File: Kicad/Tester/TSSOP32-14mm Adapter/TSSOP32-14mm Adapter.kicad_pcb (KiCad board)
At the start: 2 copper layers, 18.3 x 41.4 mm, 4 parts, among them IC1 SST39VF010-70-4I-WHE, J1 Conn_02x16_Counter_Clockwise, J4 Pin_Header_01x16, J5 Pin_Header_01x16

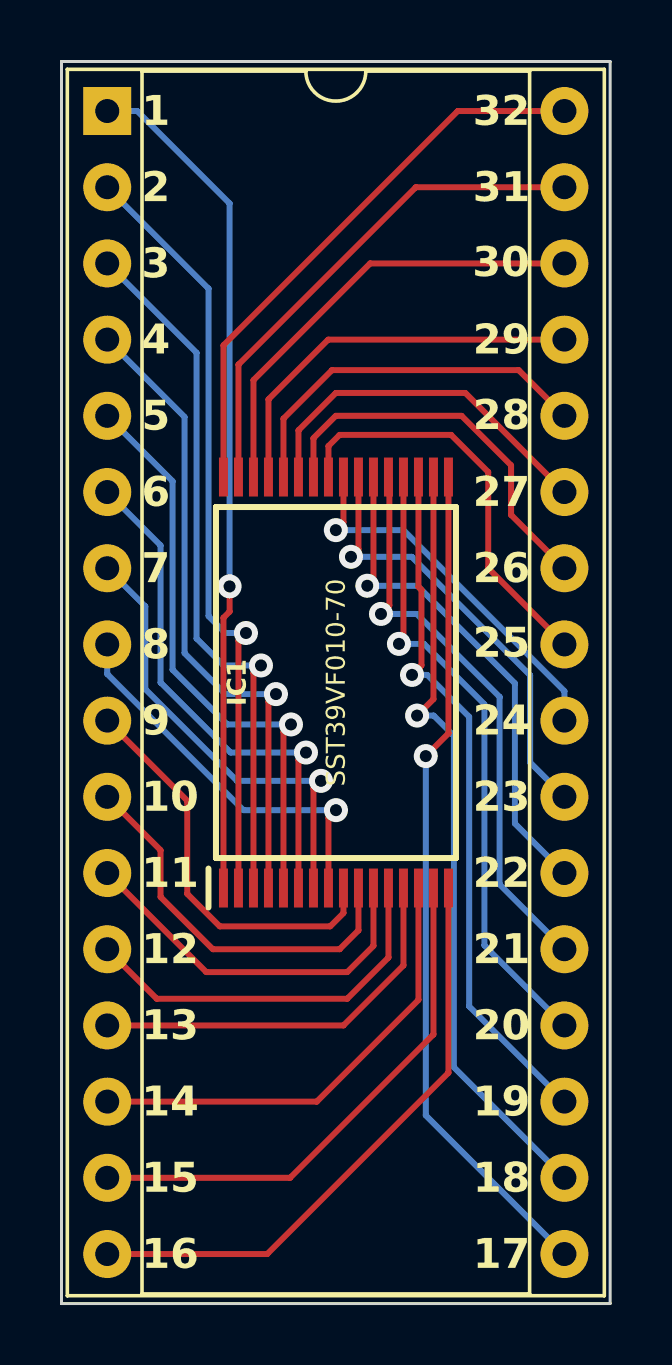
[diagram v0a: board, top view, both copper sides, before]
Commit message: Converted LCD testers to Kicad 9.0.
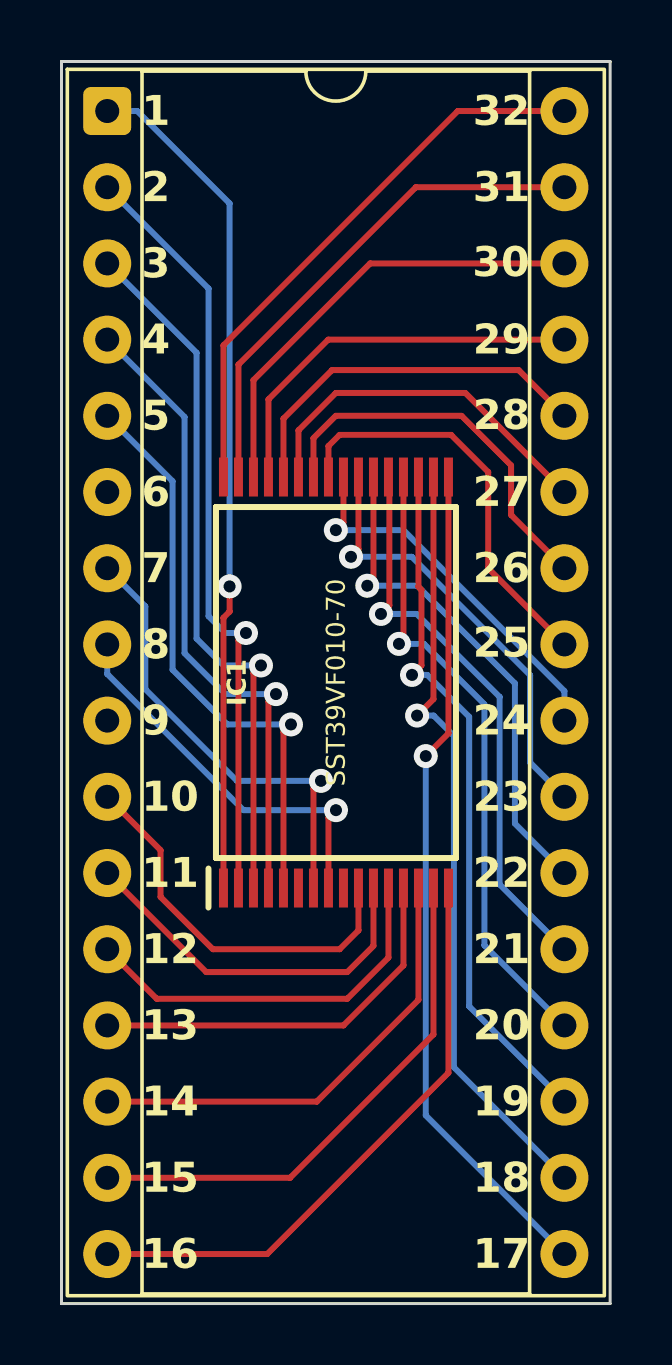
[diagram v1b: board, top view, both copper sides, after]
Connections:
- IC1 pad 6: /6 -> unconnected-(IC1-N.C.-Pad6)
- IC1 pad 9: /9 -> unconnected-(IC1-N.C.-Pad9)
- J1 pad 6: /6 -> unconnected-(J1-Pin_6-Pad6)
- J1 pad 9: /9 -> unconnected-(J1-Pin_9-Pad9)
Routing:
- net /6: track 17.5 -> 0.00 mm, vias 1 -> 0
- net /9: track 13.6 -> 0.00 mm
